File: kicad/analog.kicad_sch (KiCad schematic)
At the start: 23 parts, among them J26 ADC #1 in 2, J27 ADC #1 in 3, J37 ADC #1 in 0, J38 ADC #1 in 1, U5 ADS1115IDGSR

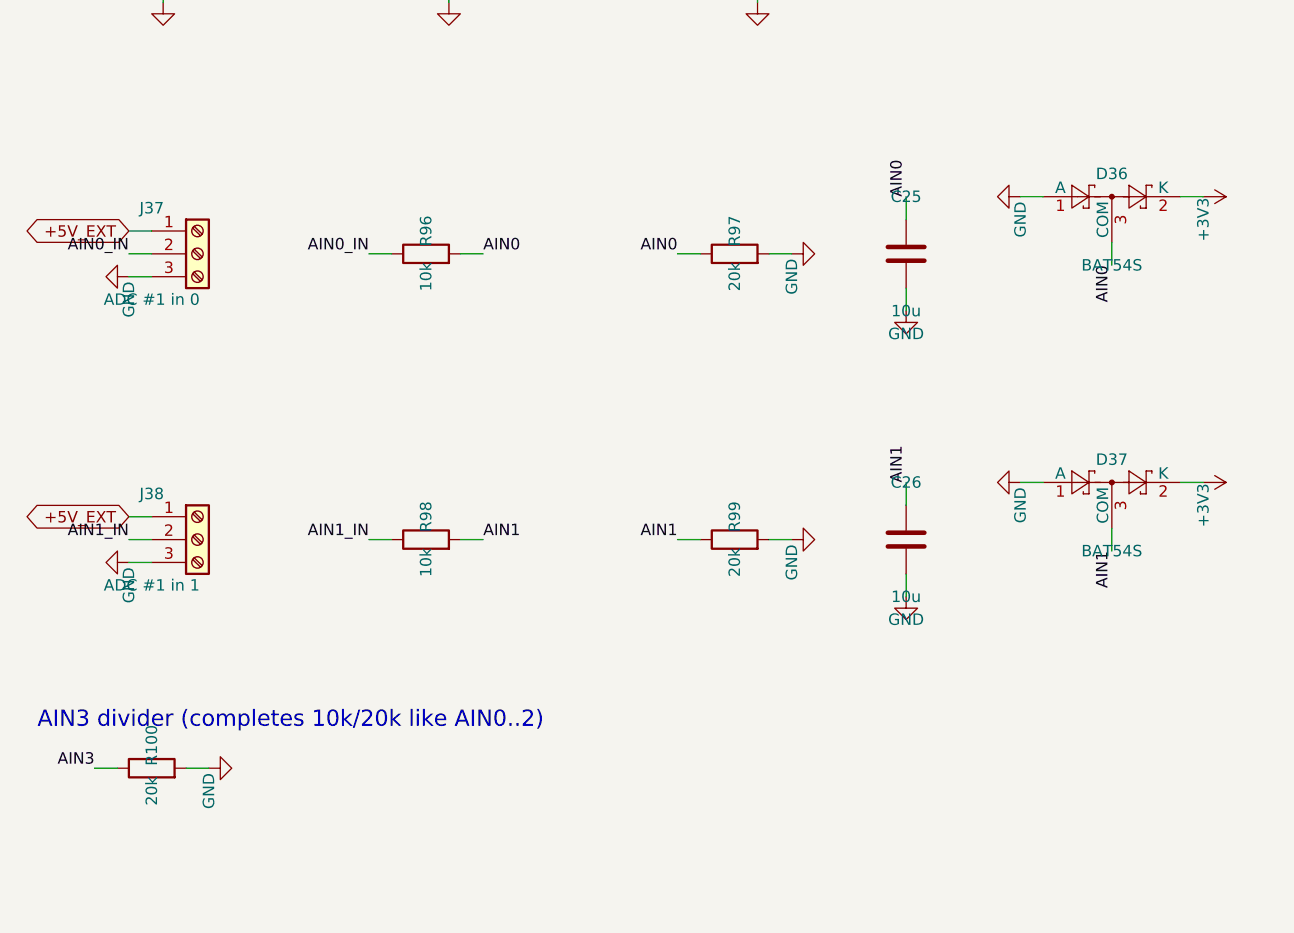
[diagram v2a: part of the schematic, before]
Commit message: kicad: v2 space measures - feeder on power bar header, resistor arrays, 0603, TSSOP buffers
Feeder port dropped: power bar header pin 10 = +3V3_EXT (own AMS1117), any PCA #2 channel as signal; 30 series resistors as 8x 4x0603 arrays; new passives 0603; new 74HCT244 in TSSOP-20; flat parts may use the Pi zone, connectors anywhere else. ERC 0, DRC copper 0, parity 0.

Co-Authored-By: Claude Opus 5.5 <noreply@anthropic.com>
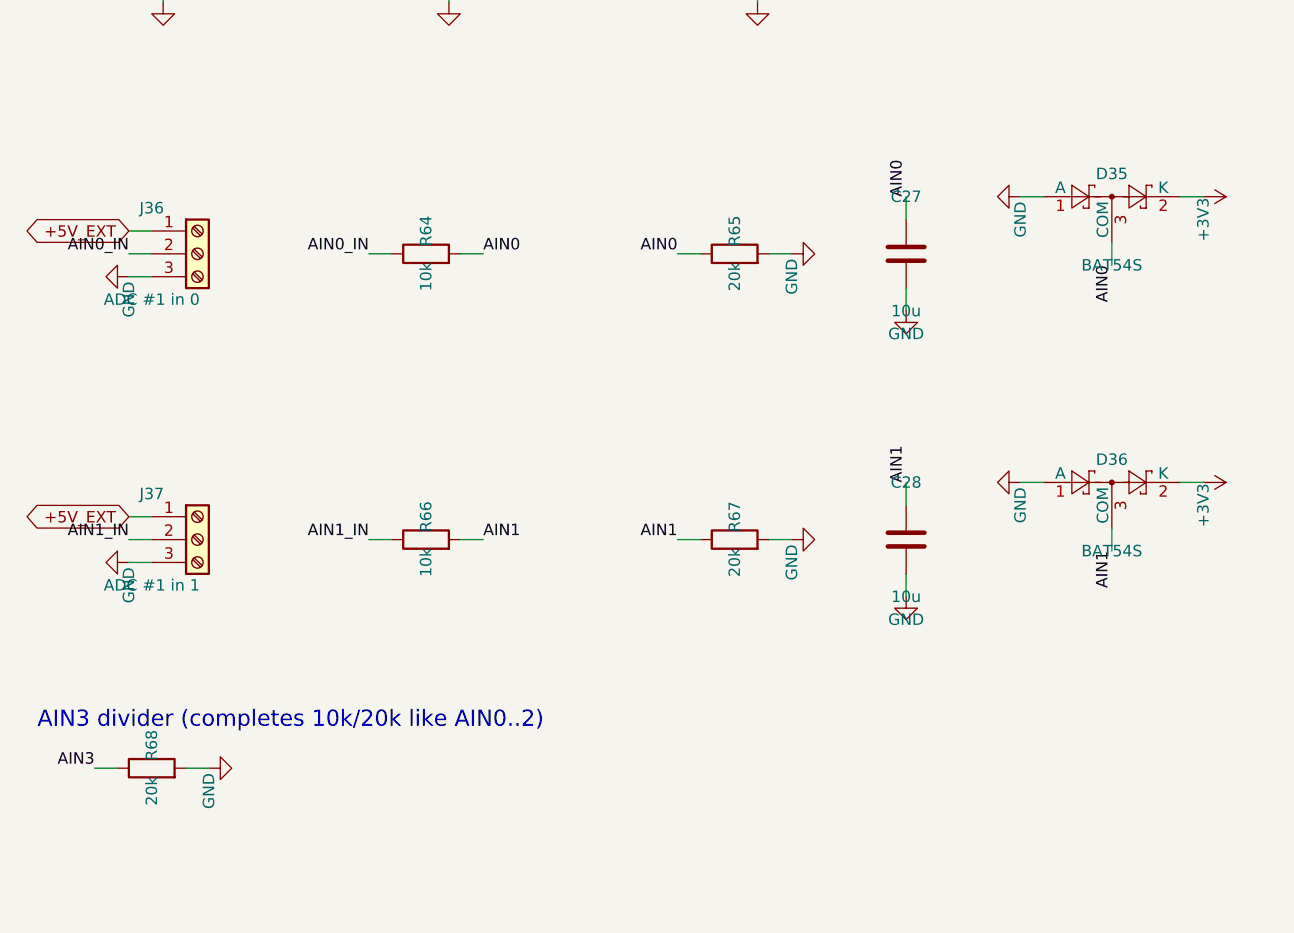
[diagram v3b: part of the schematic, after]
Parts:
- removed C25, C26: 10u, Capacitor_SMD:C_0805_2012Metric, symbol Device:C
- removed D37: BAT54S, Package_TO_SOT_SMD:SOT-23, symbol Diode:BAT54S
- removed J38: ADC #1 in 1, aquaPCB:TerminalBlock_Kangnex_WJ250B-3.5-03P_P3.50mm_Staggered, symbol Connector:Screw_Terminal_01x03
- removed R100, R97, R99: 20k, Resistor_SMD:R_0805_2012Metric, symbol Device:R
- removed R96, R98: 10k, Resistor_SMD:R_0805_2012Metric, symbol Device:R
- added C27, C28: 10u, Capacitor_SMD:C_0603_1608Metric, symbol Device:C
- added D35: BAT54S, Package_TO_SOT_SMD:SOT-23, symbol Diode:BAT54S
- added J36: ADC #1 in 0, aquaPCB:TerminalBlock_Kangnex_WJ250B-3.5-03P_P3.50mm_Staggered, symbol Connector:Screw_Terminal_01x03
- added R64, R66: 10k, Resistor_SMD:R_0603_1608Metric, symbol Device:R
- added R65, R67, R68: 20k, Resistor_SMD:R_0603_1608Metric, symbol Device:R
- J37: value ADC #1 in 0 -> ADC #1 in 1
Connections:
- net +3V3: now also D35.2 (K)
- net +5V_EXT: now also J36.1 (Pin_1)
- net AIN0: now also C27.1, D35.3 (COM), R64.2, R65.1; no longer D36.3 (COM)
- net AIN0_IN: now also J36.2 (Pin_2), R64.1; no longer J37.2 (Pin_2)
- net AIN1: now also D36.3 (COM), C28.1, R66.2, R67.1
- net AIN1_IN: now also J37.2 (Pin_2), R66.1
- net AIN3: now also R68.1
- net GND: now also C27.2, C28.2, D35.1 (A), J36.3 (Pin_3), R65.2, R67.2, R68.2
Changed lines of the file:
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@@
 		(on_board yes)
 		(dnp no)
-		(property "Reference" "J37"
+		(property "Reference" "J36"
 			(at 38.1 96.52 0)
 			(effects
@@
 			(project "aquaPCB"
 				(path "/80232f81-1179-4777-a7f0-674a974d53cc/7f54e82c-99a9-49f3-9f13-2c730539fa02"
-					(reference "J37")
+					(reference "J36")
 					(unit 1)))))
 	(wire
@@
 		(on_board no)
 		(dnp no)
-		(property "Reference" "#PWR234"
+		(property "Reference" "#PWR232"
 			(at 35.56 101.6 0)
 			(effects
@@
 			(project "aquaPCB"
 				(path "/80232f81-1179-4777-a7f0-674a974d53cc/7f54e82c-99a9-49f3-9f13-2c730539fa02"
-					(reference "#PWR234")
+					(reference "#PWR232")
 					(unit 1)))))
 	(symbol
@@
 		(on_board yes)
 		(dnp no)
-		(property "Reference" "R96"
+		(property "Reference" "R64"
 			(at 68.58 99.06 0)
 			(effects
@@
 				(font
 					(size 1.27 1.27))))
-		(property "Footprint" "Resistor_SMD:R_0805_2012Metric"
+		(property "Footprint" "Resistor_SMD:R_0603_1608Metric"
 			(at 68.58 101.6 0)
 			(effects
@@
 					(size 1.27 1.27))
 				(hide yes)))
-		(property "LCSC" "C17414"
+		(property "LCSC" "C25804"
 			(at 68.58 101.6 0)
 			(effects
@@
 			(project "aquaPCB"
 				(path "/80232f81-1179-4777-a7f0-674a974d53cc/7f54e82c-99a9-49f3-9f13-2c730539fa02"
-					(reference "R96")
+					(reference "R64")
 					(unit 1)))))
 	(wire
@@
 		(on_board yes)
 		(dnp no)
-		(property "Reference" "R97"
+		(property "Reference" "R65"
 			(at 102.87 99.06 0)
 			(effects
@@
 				(font
 					(size 1.27 1.27))))
-		(property "Footprint" "Resistor_SMD:R_0805_2012Metric"
+		(property "Footprint" "Resistor_SMD:R_0603_1608Metric"
 			(at 102.87 101.6 0)
 			(effects
@@
 					(size 1.27 1.27))
 				(hide yes)))
-		(property "LCSC" "C4328"
+		(property "LCSC" "C4184"
 			(at 102.87 101.6 0)
 			(effects
@@
 			(project "aquaPCB"
 				(path "/80232f81-1179-4777-a7f0-674a974d53cc/7f54e82c-99a9-49f3-9f13-2c730539fa02"
-					(reference "R97")
+					(reference "R65")
 					(unit 1)))))
 	(wire
@@
 		(on_board no)
 		(dnp no)
-		(property "Reference" "#PWR235"
+		(property "Reference" "#PWR233"
 			(at 109.22 99.06 0)
 			(effects
@@
 			(project "aquaPCB"
 				(path "/80232f81-1179-4777-a7f0-674a974d53cc/7f54e82c-99a9-49f3-9f13-2c730539fa02"
-					(reference "#PWR235")
+					(reference "#PWR233")
 					(unit 1)))))
 	(symbol
@@
 		(on_board yes)
 		(dnp no)
-		(property "Reference" "C25"
+		(property "Reference" "C27"
 			(at 121.92 95.25 0)
 			(effects
@@
 				(font
 					(size 1.27 1.27))))
-		(property "Footprint" "Capacitor_SMD:C_0805_2012Metric"
+		(property "Footprint" "Capacitor_SMD:C_0603_1608Metric"
 			(at 121.92 101.6 0)
 			(effects
@@
 					(size 1.27 1.27))
 				(hide yes)))
-		(property "LCSC" "C15850"
+		(property "LCSC" "C19702"
 			(at 121.92 101.6 0)
 			(effects
@@
 			(project "aquaPCB"
 				(path "/80232f81-1179-4777-a7f0-674a974d53cc/7f54e82c-99a9-49f3-9f13-2c730539fa02"
-					(reference "C25")
+					(reference "C27")
 					(unit 1)))))
 	(wire
@@
 		(on_board no)
 		(dnp no)
-		(property "Reference" "#PWR236"
+		(property "Reference" "#PWR234"
 			(at 121.92 105.41 0)
 			(effects
@@
 			(project "aquaPCB"
 				(path "/80232f81-1179-4777-a7f0-674a974d53cc/7f54e82c-99a9-49f3-9f13-2c730539fa02"
-					(reference "#PWR236")
+					(reference "#PWR234")
 					(unit 1)))))
 	(symbol
@@
 		(on_board yes)
 		(dnp no)
-		(property "Reference" "D36"
+		(property "Reference" "D35"
 			(at 144.78 92.71 0)
 			(effects
@@
 			(project "aquaPCB"
 				(path "/80232f81-1179-4777-a7f0-674a974d53cc/7f54e82c-99a9-49f3-9f13-2c730539fa02"
-					(reference "D36")
+					(reference "D35")
 					(unit 1)))))
 	(wire
@@
 		(on_board no)
 		(dnp no)
-		(property "Reference" "#PWR237"
+		(property "Reference" "#PWR235"
 			(at 134.62 92.71 0)
 			(effects
@@
 			(project "aquaPCB"
 				(path "/80232f81-1179-4777-a7f0-674a974d53cc/7f54e82c-99a9-49f3-9f13-2c730539fa02"
-					(reference "#PWR237")
+					(reference "#PWR235")
 					(unit 1)))))
 	(wire
@@
 		(on_board no)
 		(dnp no)
-		(property "Reference" "#PWR238"
+		(property "Reference" "#PWR236"
 			(at 154.94 92.71 0)
 			(effects
@@
 			(project "aquaPCB"
 				(path "/80232f81-1179-4777-a7f0-674a974d53cc/7f54e82c-99a9-49f3-9f13-2c730539fa02"
-					(reference "#PWR238")
+					(reference "#PWR236")
 					(unit 1)))))
 	(wire
@@
 		(on_board yes)
 		(dnp no)
-		(property "Reference" "J38"
+		(property "Reference" "J37"
 			(at 38.1 128.27 0)
 			(effects
@@
 			(project "aquaPCB"
 				(path "/80232f81-1179-4777-a7f0-674a974d53cc/7f54e82c-99a9-49f3-9f13-2c730539fa02"
-					(reference "J38")
+					(reference "J37")
 					(unit 1)))))
 	(wire
@@
 		(on_board no)
 		(dnp no)
-		(property "Reference" "#PWR239"
+		(property "Reference" "#PWR237"
 			(at 35.56 133.35 0)
 			(effects
@@
 			(project "aquaPCB"
 				(path "/80232f81-1179-4777-a7f0-674a974d53cc/7f54e82c-99a9-49f3-9f13-2c730539fa02"
-					(reference "#PWR239")
+					(reference "#PWR237")
 					(unit 1)))))
 	(symbol
@@
 		(on_board yes)
 		(dnp no)
-		(property "Reference" "R98"
+		(property "Reference" "R66"
 			(at 68.58 130.81 0)
 			(effects
@@
 				(font
 					(size 1.27 1.27))))
-		(property "Footprint" "Resistor_SMD:R_0805_2012Metric"
+		(property "Footprint" "Resistor_SMD:R_0603_1608Metric"
 			(at 68.58 133.35 0)
 			(effects
@@
 					(size 1.27 1.27))
 				(hide yes)))
-		(property "LCSC" "C17414"
+		(property "LCSC" "C25804"
 			(at 68.58 133.35 0)
 			(effects
@@
 			(project "aquaPCB"
 				(path "/80232f81-1179-4777-a7f0-674a974d53cc/7f54e82c-99a9-49f3-9f13-2c730539fa02"
-					(reference "R98")
+					(reference "R66")
 					(unit 1)))))
 	(wire
@@
 		(on_board yes)
 		(dnp no)
-		(property "Reference" "R99"
+		(property "Reference" "R67"
 			(at 102.87 130.81 0)
 			(effects
@@
 				(font
 					(size 1.27 1.27))))
-		(property "Footprint" "Resistor_SMD:R_0805_2012Metric"
+		(property "Footprint" "Resistor_SMD:R_0603_1608Metric"
 			(at 102.87 133.35 0)
 			(effects
@@
 					(size 1.27 1.27))
 				(hide yes)))
-		(property "LCSC" "C4328"
+		(property "LCSC" "C4184"
 			(at 102.87 133.35 0)
 			(effects
@@
 			(project "aquaPCB"
 				(path "/80232f81-1179-4777-a7f0-674a974d53cc/7f54e82c-99a9-49f3-9f13-2c730539fa02"
-					(reference "R99")
+					(reference "R67")
 					(unit 1)))))
 	(wire
@@
 		(on_board no)
 		(dnp no)
-		(property "Reference" "#PWR240"
+		(property "Reference" "#PWR238"
 			(at 109.22 130.81 0)
 			(effects
@@
 			(project "aquaPCB"
 				(path "/80232f81-1179-4777-a7f0-674a974d53cc/7f54e82c-99a9-49f3-9f13-2c730539fa02"
-					(reference "#PWR240")
+					(reference "#PWR238")
 					(unit 1)))))
 	(symbol
@@
 		(on_board yes)
 		(dnp no)
-		(property "Reference" "C26"
+		(property "Reference" "C28"
 			(at 121.92 127 0)
 			(effects
@@
 				(font
 					(size 1.27 1.27))))
-		(property "Footprint" "Capacitor_SMD:C_0805_2012Metric"
+		(property "Footprint" "Capacitor_SMD:C_0603_1608Metric"
 			(at 121.92 133.35 0)
 			(effects
@@
 					(size 1.27 1.27))
 				(hide yes)))
-		(property "LCSC" "C15850"
+		(property "LCSC" "C19702"
 			(at 121.92 133.35 0)
 			(effects
@@
 			(project "aquaPCB"
 				(path "/80232f81-1179-4777-a7f0-674a974d53cc/7f54e82c-99a9-49f3-9f13-2c730539fa02"
-					(reference "C26")
+					(reference "C28")
 					(unit 1)))))
 	(wire
@@
 		(on_board no)
 		(dnp no)
-		(property "Reference" "#PWR241"
+		(property "Reference" "#PWR239"
 			(at 121.92 137.16 0)
 			(effects
@@
 			(project "aquaPCB"
 				(path "/80232f81-1179-4777-a7f0-674a974d53cc/7f54e82c-99a9-49f3-9f13-2c730539fa02"
-					(reference "#PWR241")
+					(reference "#PWR239")
 					(unit 1)))))
 	(symbol
@@
 		(on_board yes)
 		(dnp no)
-		(property "Reference" "D37"
+		(property "Reference" "D36"
 			(at 144.78 124.46 0)
 			(effects
@@
 			(project "aquaPCB"
 				(path "/80232f81-1179-4777-a7f0-674a974d53cc/7f54e82c-99a9-49f3-9f13-2c730539fa02"
-					(reference "D37")
+					(reference "D36")
 					(unit 1)))))
 	(wire
@@
 		(on_board no)
 		(dnp no)
-		(property "Reference" "#PWR242"
+		(property "Reference" "#PWR240"
 			(at 134.62 124.46 0)
 			(effects
@@
 			(project "aquaPCB"
 				(path "/80232f81-1179-4777-a7f0-674a974d53cc/7f54e82c-99a9-49f3-9f13-2c730539fa02"
-					(reference "#PWR242")
+					(reference "#PWR240")
 					(unit 1)))))
 	(wire
@@
 		(on_board no)
 		(dnp no)
-		(property "Reference" "#PWR243"
+		(property "Reference" "#PWR241"
 			(at 154.94 124.46 0)
 			(effects
@@
 			(project "aquaPCB"
 				(path "/80232f81-1179-4777-a7f0-674a974d53cc/7f54e82c-99a9-49f3-9f13-2c730539fa02"
-					(reference "#PWR243")
+					(reference "#PWR241")
 					(unit 1)))))
 	(wire
@@
 		(on_board yes)
 		(dnp no)
-		(property "Reference" "R100"
+		(property "Reference" "R68"
 			(at 38.1 156.21 0)
 			(effects
@@
 				(font
 					(size 1.27 1.27))))
-		(property "Footprint" "Resistor_SMD:R_0805_2012Metric"
+		(property "Footprint" "Resistor_SMD:R_0603_1608Metric"
 			(at 38.1 158.75 0)
 			(effects
@@
 					(size 1.27 1.27))
 				(hide yes)))
-		(property "LCSC" "C4328"
+		(property "LCSC" "C4184"
 			(at 38.1 158.75 0)
 			(effects
@@
 			(project "aquaPCB"
 				(path "/80232f81-1179-4777-a7f0-674a974d53cc/7f54e82c-99a9-49f3-9f13-2c730539fa02"
-					(reference "R100")
+					(reference "R68")
 					(unit 1)))))
 	(wire
@@
 		(on_board no)
 		(dnp no)
-		(property "Reference" "#PWR244"
+		(property "Reference" "#PWR242"
 			(at 44.45 156.21 0)
 			(effects
@@
 			(project "aquaPCB"
 				(path "/80232f81-1179-4777-a7f0-674a974d53cc/7f54e82c-99a9-49f3-9f13-2c730539fa02"
-					(reference "#PWR244")
+					(reference "#PWR242")
 					(unit 1)))))
 	(text "AIN3 divider (completes 10k/20k like AIN0..2)"
